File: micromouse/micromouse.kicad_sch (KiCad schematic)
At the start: 0 parts

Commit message: added mpu 6050 schematic
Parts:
- added C1: 0.1, symbol Device:C
- added U1: MPU-6050, QFN24_4X4X0P9-0P5_TDK, symbol mpu-6060-gyroscope:MPU-6050
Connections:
- new net +3.3V: C1.1, U1.9 (AD0)
- new net GND: C1.2, U1.18 (GND)
- new net SCL: U1.23 (SCL)
- new net SDA: U1.24 (SDA)

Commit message: update
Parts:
- added C2: 10uF, 10uF-ceramic-capacitor:CAPC2012X135N, symbol 10ufCeramicCapacitor:GRM21BR61C106KE15L
- added C2: 22uF, 22uF-ceramic-capacitor:CAPC1608X105N, symbol 22ufCeramicCapacitor:CL10A226MP8NUNE
- added C3: 10 uF, symbol Device:C
- added C3, C4, C5: 4.7 uF, symbol Device:C
- added C4, C6: 0.1 uF, symbol Device:C
- added J1, J2: B2B-PH-K-S, Connector_JST:JST_PH_B2B-PH-K_1x02_P2.00mm_Vertical, symbol B2B-PH-K-S:B2B-PH-K-S
- added J3, J4: Left Header, symbol Connector:Conn_01x06_Pin
- added LED1: INL-5AMIR15, LED_INL-5AMIR15_INO, symbol ir-emitter:INL-5AMIR15
- added Q1: SFH_313_FA-3_4, SFH_313_FA-3_4:XDCR_SFH_313_FA-3_4, symbol ir-reciever:SFH_313_FA-3_4
- added R1: 47k, symbol Device:R_US
- added R2: 51 ohm, symbol Device:R_US
- added R3: 100 ohm, symbol Device:R_US
- added R4: 1.8k, symbol Device:R_US
- added U2: AZ1117IH-3.3TRG1, voltage regulator:SOT230P700X185-4N, symbol AZ1117IH-3.3TRG1:AZ1117IH-3.3TRG1
- added U3: L293DD, L293DD:SOIC127P1032X265-20N, symbol L293DD:L293DD
- added U4: BS170, TO_SA06_ONS, symbol nchannelmosfet-mm:BS170
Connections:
- net GND: now also C2.2, C2.2, C4.2, C4.2, C6.2, J2.2, J3.1 (Pin_1), J4.1 (Pin_1), R1.1, R1.2, R3.2, R4.2, U2.1 (GND), U4.3 (S)
- new net: LED1.1, U4.2 (D)
- new net: LED1.2, R2.2
- new net: J1.2, J2.1
- new net 3V3: C2.1, C5.1, C6.1, J3.4 (Pin_4), J4.4 (Pin_4), Q1.2, R2.1, U2.2 (OUTPUT), U2.4 (VOUT), U3.1 (ENABLE_1), U3.11 (ENABLE_2)
- new net LENC1: J3.2 (Pin_2)
- new net LENC2: J3.3 (Pin_3)
- new net MGND: C3.1, C3.1, U3.14 (GND__4), U3.15 (GND__5), U3.16 (GND__6), U3.17 (GND__7), U3.4 (GND), U3.5 (GND__1), U3.6 (GND__2), U3.7 (GND__3)
- new net ML1: J3.6 (Pin_6), U3.8 (OUTPUT_2)
- new net ML2: J3.5 (Pin_5), U3.3 (OUTPUT_1)
- new net MR1: J4.6 (Pin_6), U3.18 (OUTPUT_4)
- new net MR2: J4.5 (Pin_5), U3.13 (OUTPUT_3)
- new net PB6: U3.2 (INPUT_1)
- new net PB7: U3.9 (INPUT_2)
- new net PB8: U3.12 (INPUT_3)
- new net PB9: U3.19 (INPUT_4)
- new net PC5: Q1.1, R4.1
- new net PC9: R3.1
- new net RENC1: J4.2 (Pin_2), J4.3 (Pin_3)
- new net VCC: C2.1, C3.2, C3.2, C4.1, C4.1, J1.1, U2.3 (INPUT), U3.10 (VS), U3.20 (VSS)

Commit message: sch updates
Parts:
- C1, C4, C6: footprint (none) -> CL21B104KBCNNNC:CAPC2012X95N
- C3: footprint (none) -> CL21B106KOQNNNE:CAPC2012X140N
- renumbered C2 to C20, C3 to C21, C4 to C22
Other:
- added sheet mcu (untitled.kicad_sch)
- moved on the sheet: C1, C2, C20, C21, C22, C3, C4, C5, C6, J1, J2, J3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

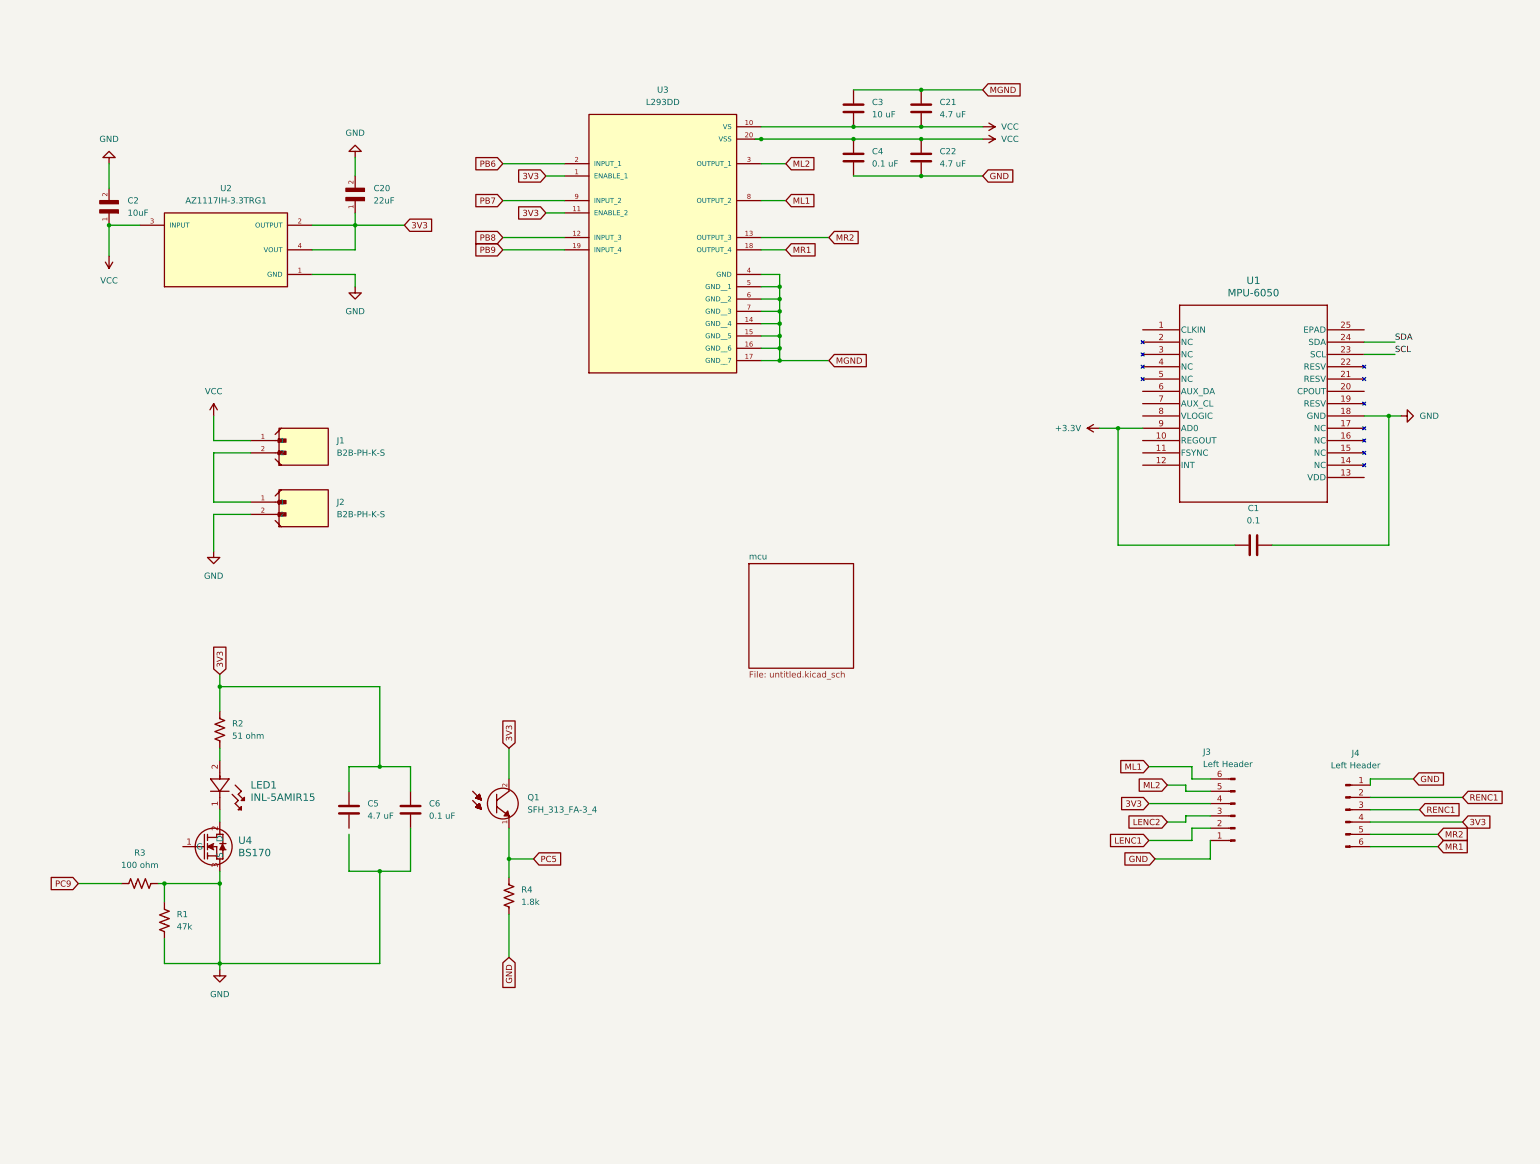
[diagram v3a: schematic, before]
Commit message: updated footprints and schematic
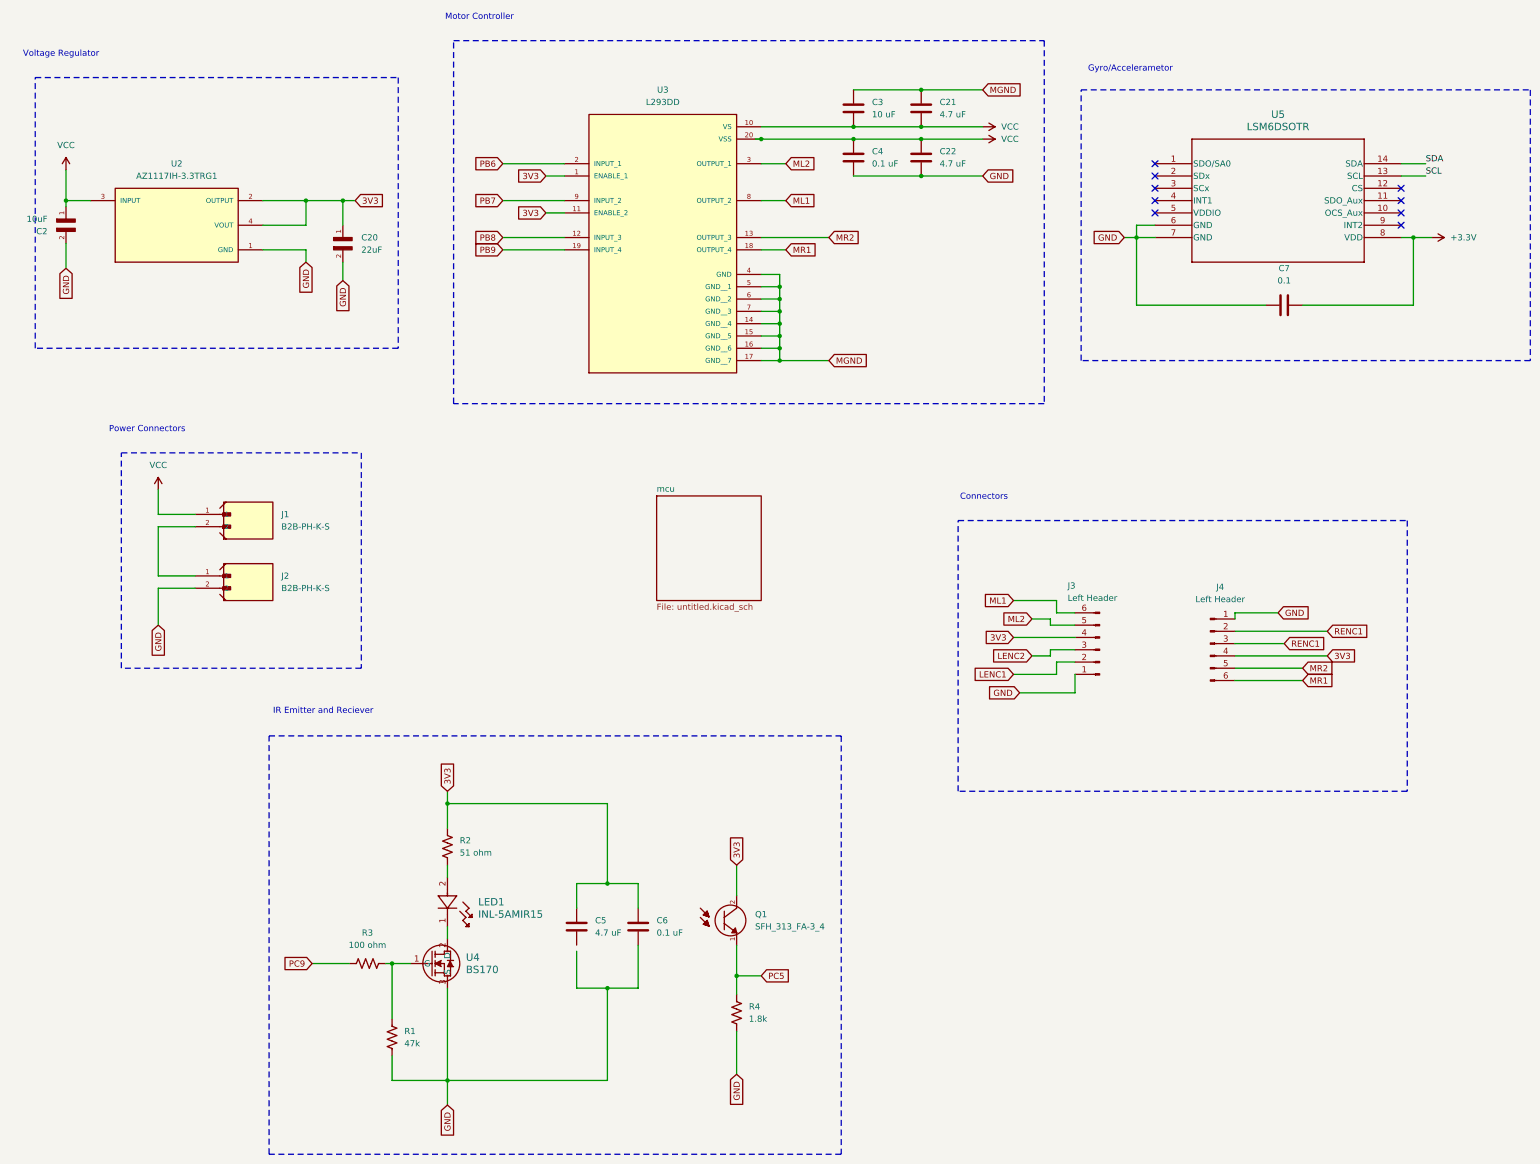
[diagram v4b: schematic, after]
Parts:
- removed C1: 0.1, CL21B104KBCNNNC:CAPC2012X95N, symbol Device:C
- removed U1: MPU-6050, QFN24_4X4X0P9-0P5_TDK, symbol mpu-6060-gyroscope:MPU-6050
- added C7: 0.1, Capacitor_SMD:C_0805_2012Metric, symbol Device:C
- added U5: LSM6DSOTR, LGA-14L_2P5X3X0P86_STM, symbol LSM6DSOTR:LSM6DSOTR
- C2: footprint 10uF-ceramic-capacitor:CAPC2012X135N -> Capacitor_SMD:C_0805_2012Metric
- C20: footprint 22uF-ceramic-capacitor:CAPC1608X105N -> Capacitor_SMD:C_0805_2012Metric
- C21, C22, C5: footprint (none) -> Capacitor_SMD:C_0805_2012Metric
- C3: footprint CL21B106KOQNNNE:CAPC2012X140N -> Capacitor_SMD:C_0805_2012Metric
- C4, C6: footprint CL21B104KBCNNNC:CAPC2012X95N -> Capacitor_SMD:C_0805_2012Metric
- J3, J4: footprint (none) -> 6x0.1connpins:SULLINS_PPTC061LFBN-RC
- LED1: footprint LED_INL-5AMIR15_INO -> ir-emitter:LED_INL-5AMIR15_INO
- Q1: footprint SFH_313_FA-3_4:XDCR_SFH_313_FA-3_4 -> ir reciever:XDCR_SFH_313_FA-3_4
- R1, R2, R3, R4: footprint (none) -> Resistor_SMD:R_0805_2012Metric
- U2: footprint voltage regulator:SOT230P700X185-4N -> AZ1117IH-3.3TRG1:SOT230P700X185-4N
- U3: footprint L293DD:SOIC127P1032X265-20N -> L293DD-motor-controller:SOIC127P1032X265-20N
- U4: footprint TO_SA06_ONS -> bs170:TO_SA06_ONS
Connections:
- net +3.3V: now also C7.2, U5.8 (VDD)
- net GND: now also C7.1, U5.6 (GND), U5.7 (GND); no longer R1.1, R3.2
- net SCL: now also U5.13 (SCL)
- net SDA: now also U5.14 (SDA)
- net at U4.1 (G): now also R1.1, R3.2
- no-connect marks 0 -> 9
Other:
- note added: "Connectors"
- note added: "Gyro/Accelerametor"
- note added: "IR Emitter and Reciever"
- note added: "Motor Controller"
- note added: "Power Connectors"
- note added: "Voltage Regulator"
- moved on the sheet: C2, C20, C5, C6, J1, J2, J3, J4, LED1, Q1, R1, R2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

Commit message: subsystem grouping
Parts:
- added LED2, LED3: LTST-C194TBKT, LEDC1608X35N, symbol blue-led:LTST-C194TBKT
- added R7: 100 ohm, Resistor_SMD:R_0805_2012Metric, symbol Device:R_US
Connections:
- net GND: now also C5.2, LED2.1 (K), LED3.1 (K); no longer R4.2
- net PC9: now also R7.1
- new net: LED3.2 (A), R4.2
- new net: LED2.2 (A), R7.2

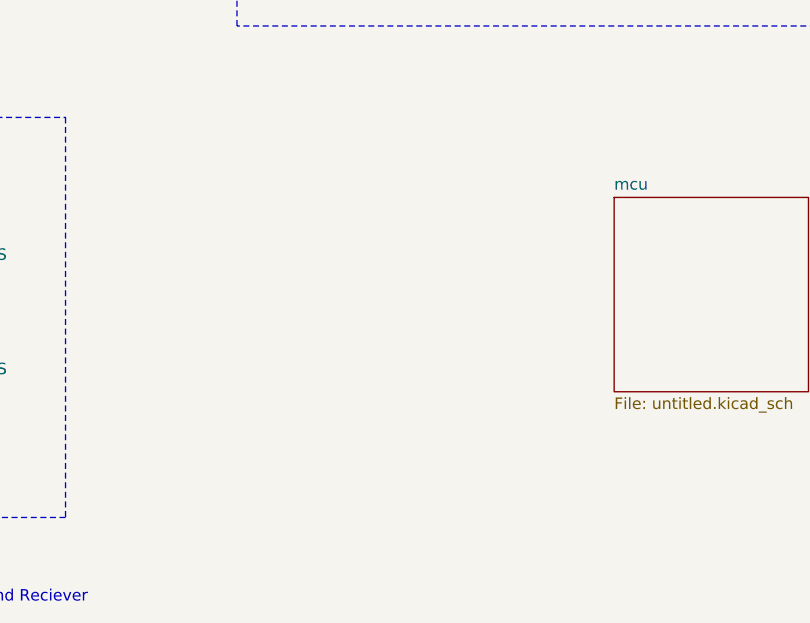
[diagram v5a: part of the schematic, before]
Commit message: Revision + adding motors
changes to schematic and pcb layout
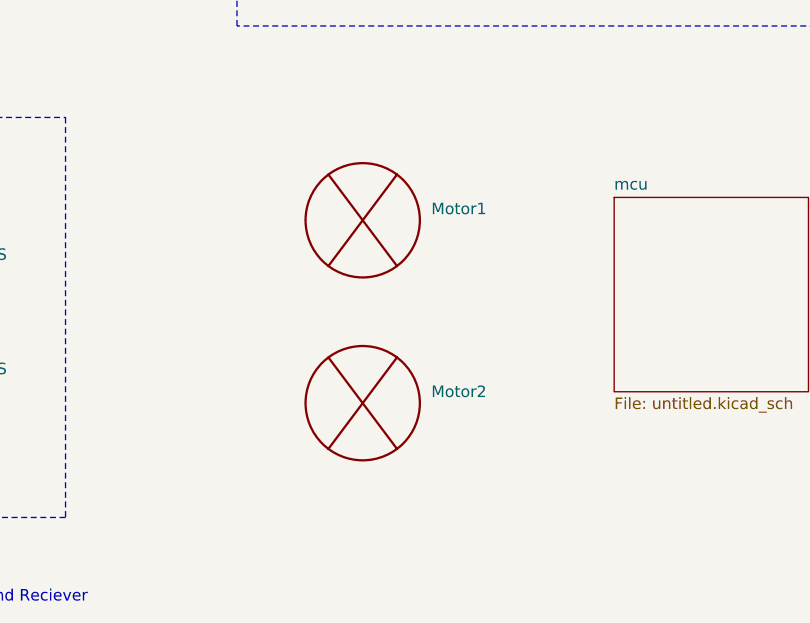
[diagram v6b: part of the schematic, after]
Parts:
- added Motor1, Motor2: ~, symbol pololu_motor:Pololu_Motor
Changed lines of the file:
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@@
+	)
+	(symbol
+		(lib_id "pololu_motor:Pololu_Motor")
+		(at 96.52 142.24 0)
+		(unit 1)
+		(exclude_from_sim no)
+		(in_bom yes)
+		(on_board yes)
+		(dnp no)
+		(fields_autoplaced yes)
+		(property "Reference" "Motor2"
+			(at 104.14 133.3499 0)
+			(effects
+				(font
+					(size 1.27 1.27)
+				)
+				(justify left)
+			)
+		)
+		(property "Value" "~"
+			(at 104.14 135.8899 0)
+			(effects
+				(font
+					(size 1.27 1.27)
+				)
+				(justify left)
+			)
+		)
+		(property "Footprint" ""
+			(at 96.52 142.24 0)
+			(effects
+				(font
+					(size 1.27 1.27)
+				)
+				(hide yes)
+			)
+		)
+		(property "Datasheet" ""
+			(at 96.52 142.24 0)
+			(effects
+				(font
+					(size 1.27 1.27)
+				)
+				(hide yes)
+			)
+		)
+		(property "Description" ""
+			(at 96.52 142.24 0)
+			(effects
+				(font
+					(size 1.27 1.27)
+				)
+				(hide yes)
+			)
+		)
+		(instances
+			(project ""
+				(path "/6f21d099-3493-45a5-8fb2-59b651d74bbe"
+					(reference "Motor2")
+					(unit 1)
+				)
+			)
+		)
 	)
 	(symbol
@@
 					(unit 1)
 				)
+			)
+		)
+	)
+	(symbol
+		(lib_id "pololu_motor:Pololu_Motor")
+		(at 96.52 121.92 0)
+		(unit 1)
+		(exclude_from_sim no)
+		(in_bom yes)
+		(on_board yes)
+		(dnp no)
+		(fields_autoplaced yes)
+		(property "Reference" "Motor1"
+			(at 104.14 113.0299 0)
+			(effects
+				(font
+					(size 1.27 1.27)
+				)
+				(justify left)
+			)
+		)
+		(property "Value" "~"
+			(at 104.14 115.5699 0)
+			(effects
+				(font
+					(size 1.27 1.27)
+				)
+				(justify left)
+			)
+		)
+		(property "Footprint" ""
+			(at 96.52 121.92 0)
+			(effects
+				(font
+					(size 1.27 1.27)
+				)
+				(hide yes)
+			)
+		)
+		(property "Datasheet" ""
+			(at 96.52 121.92 0)
+			(effects
+				(font
+					(size 1.27 1.27)
+				)
+				(hide yes)
+			)
+		)
+		(property "Description" ""
+			(at 96.52 121.92 0)
+			(effects
+				(font
+					(size 1.27 1.27)
+				)
+				(hide yes)
+			)
+		)
+		(instances
+			(project ""
+				(path "/6f21d099-3493-45a5-8fb2-59b651d74bbe"
+					(reference "Motor1")
+					(unit 1)
+				)

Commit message: updates to layout
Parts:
- removed C5: 4.7 uF, Capacitor_SMD:C_0805_2012Metric, symbol Device:C
- removed C6: 0.1 uF, Capacitor_SMD:C_0805_2012Metric, symbol Device:C
- removed LED1: INL-5AMIR15, ir-emitter:LED_INL-5AMIR15_INO, symbol ir-emitter:INL-5AMIR15
- removed LED2, LED3: LTST-C194TBKT, LEDC1608X35N, symbol blue-led:LTST-C194TBKT
- removed Q1: SFH_313_FA-3_4, ir reciever:XDCR_SFH_313_FA-3_4, symbol ir-reciever:SFH_313_FA-3_4
- removed R1: 47k, Resistor_SMD:R_0805_2012Metric, symbol Device:R_US
- removed R2: 51 ohm, Resistor_SMD:R_0805_2012Metric, symbol Device:R_US
- removed R3, R7: 100 ohm, Resistor_SMD:R_0805_2012Metric, symbol Device:R_US
- removed R4: 1.8k, Resistor_SMD:R_0805_2012Metric, symbol Device:R_US
- removed U4: BS170, bs170:TO_SA06_ONS, symbol nchannelmosfet-mm:BS170
- added SW2: EG1218, SW_1218_EWI, symbol power-switch:EG1218
- Motor1, Motor2: footprint (none) -> Pololu_Motor:Pololu_Motor
- U5: footprint LGA-14L_2P5X3X0P86_STM -> LSM6DSOTR:LGA-14L_2P5X3X0P86_STM
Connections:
- net GND: now also SW2.2
- net VCC: now also SW2.3; no longer J1.1
- new net: J1.1, SW2.1
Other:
- added sheet ir-emitters-receivers (ir-emitter-receiver.kicad_sch)
- sheet mcu: file untitled.kicad_sch -> mcu.kicad_sch
- note removed: "IR Emitter and Reciever"

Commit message: pcb updates
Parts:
- SW2: footprint SW_1218_EWI -> power-switch:SW_1218_EWI
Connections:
- net +3.3V is gone; now on net 3V3: C7.2, U5.8 (VDD)
- net RENC1: no longer J4.3 (Pin_3)
- net PB6 renamed PA6
- net PB7 renamed PA7
- net PB8 renamed PA3
- new net RENC2: J4.3 (Pin_3)
